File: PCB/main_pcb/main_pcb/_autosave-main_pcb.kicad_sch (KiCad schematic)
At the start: 50 parts, among them J1 Conn_01x20_Socket, J2 Conn_01x20_Socket, SW0_Header1 B6B-XH-A, SW1_Header1 B6B-XH-A

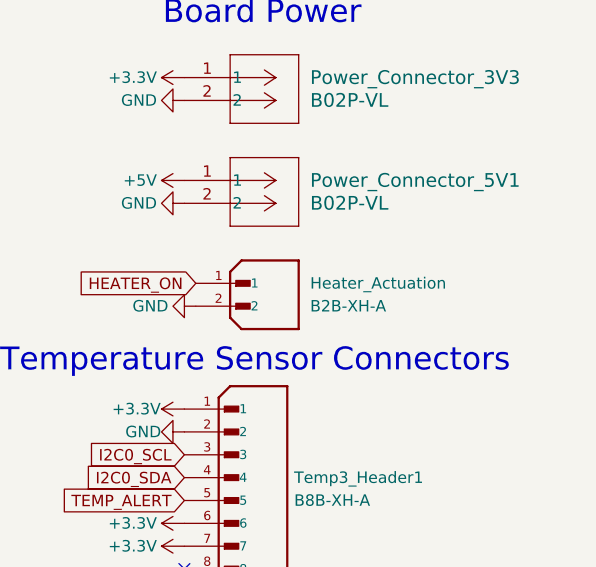
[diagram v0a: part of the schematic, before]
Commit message: Added heater actuation header.
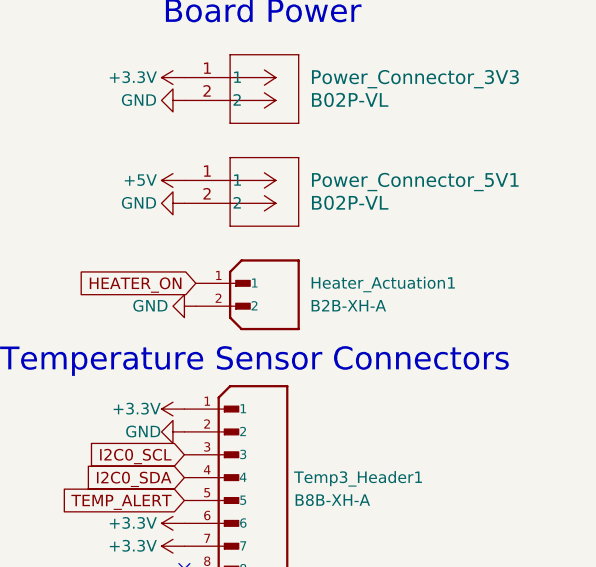
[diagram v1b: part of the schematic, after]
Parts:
- renumbered Heater_Actuation to Heater_Actuation1
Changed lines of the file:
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@@
 		(dnp no)
 		(fields_autoplaced yes)
-		(property "Reference" "Heater_Actuation"
+		(property "Reference" "Heater_Actuation1"
 			(at 382.27 46.9899 0)
 			(effects
@@
 			(project ""
 				(path "/9e1b86fa-37cc-48d2-968d-4a7578d4873f"
-					(reference "Heater_Actuation")
+					(reference "Heater_Actuation1")
 					(unit 1)
 				)
